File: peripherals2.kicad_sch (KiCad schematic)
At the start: 34 parts, among them J8 MSD-4-A, J9 DISPLAY CONN, Q3 SL2301S, Q4 T2N7002AK,LM, U7 GSDA213

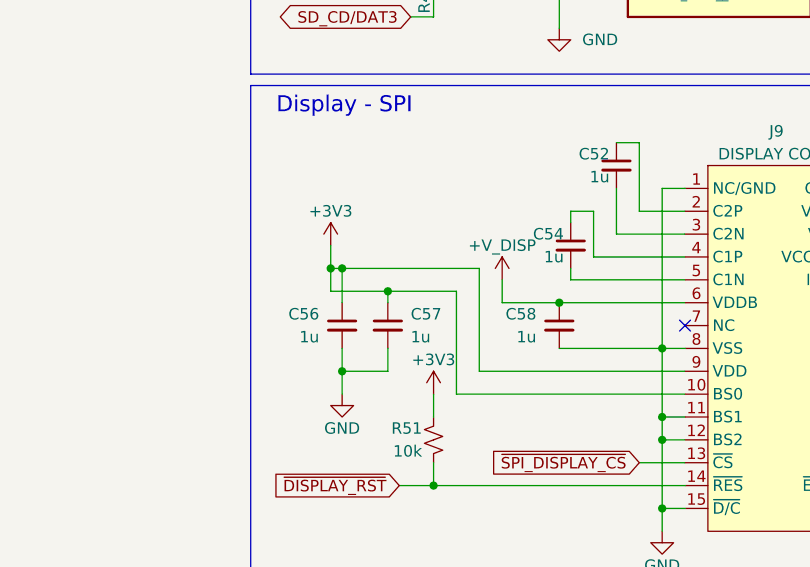
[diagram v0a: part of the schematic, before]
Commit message: Revert "refac: changes peripherals2 placement a bit"
This reverts commit 93e1f0bf6a0797c7dbeceb6b97671e5315e8a9c5.
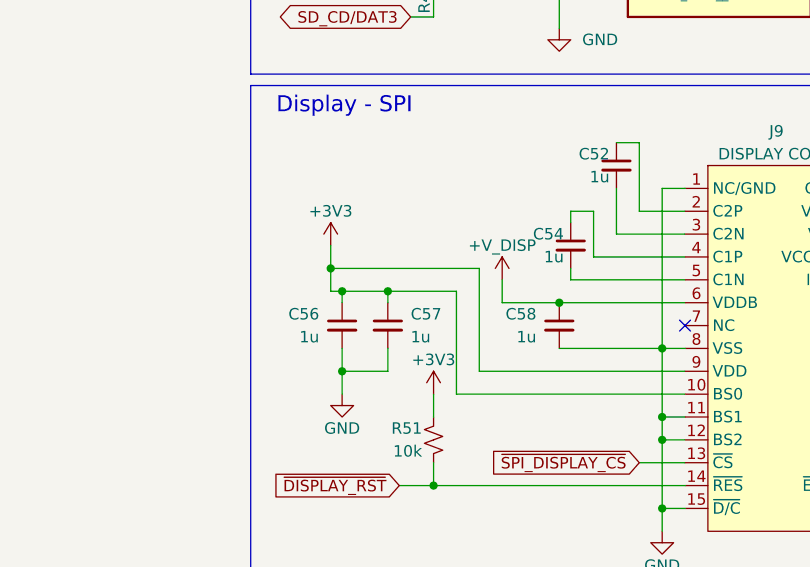
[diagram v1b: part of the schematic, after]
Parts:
- C53: footprint Capacitor_SMD:C_0402_1005Metric -> Capacitor_SMD:C_0603_1608Metric; MPN CL05A225KO5NQNC -> CL10B225KP8NNNC
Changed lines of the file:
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@@
-	)
-	(junction
-		(at 72.39 125.73)
-		(diameter 0)
-		(color 0 0 0 0)
 	)
 	(junction
@@
 	)
 	(junction
+		(at 72.39 128.27)
+		(diameter 0)
+		(color 0 0 0 0)
+	)
+	(junction
 		(at 133.35 119.38)
 		(diameter 0)
@@
 	(wire
 		(pts
-			(xy 72.39 125.73) (xy 87.63 125.73)
-		)
-		(stroke
-			(width 0)
-			(type default)
-		)
-	)
-	(wire
-		(pts
 			(xy 181.61 53.34) (xy 182.88 53.34)
 		)
@@
 	(wire
 		(pts
-			(xy 72.39 125.73) (xy 72.39 129.54)
-		)
-		(stroke
-			(width 0)
-			(type default)
-		)
-	)
-	(wire
-		(pts
 			(xy 130.81 147.32) (xy 135.89 147.32)
 		)
@@
 	(wire
 		(pts
+			(xy 72.39 128.27) (xy 77.47 128.27)
+		)
+		(stroke
+			(width 0)
+			(type default)
+		)
+	)
+	(wire
+		(pts
 			(xy 105.41 111.76) (xy 102.87 111.76)
 		)
@@
 	(wire
 		(pts
-			(xy 71.12 128.27) (xy 77.47 128.27)
+			(xy 71.12 128.27) (xy 72.39 128.27)
 		)
 		(stroke
@@
 	(wire
 		(pts
+			(xy 72.39 128.27) (xy 72.39 129.54)
+		)
+		(stroke
+			(width 0)
+			(type default)
+		)
+	)
+	(wire
+		(pts
 			(xy 158.75 86.36) (xy 149.86 86.36)
 		)
@@
 	(wire
 		(pts
-			(xy 71.12 125.73) (xy 72.39 125.73)
+			(xy 71.12 125.73) (xy 87.63 125.73)
 		)
 		(stroke
@@
 			)
 		)
-		(property "Footprint" "Capacitor_SMD:C_0402_1005Metric"
+		(property "Footprint" "Capacitor_SMD:C_0603_1608Metric"
 			(at 144.78 121.92 0)
 			(effects
@@
 			)
 		)
-		(property "Datasheet" "https://www.digikey.com.br/pt/products/detail/samsung-electro-mechanics/CL05A225KO5NQNC/3887119"
+		(property "Datasheet" "https://www.digikey.com.br/en/products/detail/samsung-electro-mechanics/CL10B225KP8NNNC/3886792"
 			(at 144.78 121.92 0)
 			(effects
@@
 			)
 		)
-		(property "MPN" "CL05A225KO5NQNC"
+		(property "MPN" "CL10B225KP8NNNC"
 			(at 144.78 121.92 0)
 			(effects

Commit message: chore: updates display capacitors
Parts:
- C53: footprint Capacitor_SMD:C_0603_1608Metric -> Capacitor_SMD:C_0402_1005Metric; MPN CL10B225KP8NNNC -> CL05A225KO5NQNC
- C55: MPN CL05A475MP5NRNC -> CL05A105KA5NQNC
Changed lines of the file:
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@@
 			)
 		)
-		(property "Footprint" "Capacitor_SMD:C_0603_1608Metric"
+		(property "Footprint" "Capacitor_SMD:C_0402_1005Metric"
 			(at 144.78 121.92 0)
 			(effects
@@
 			)
 		)
-		(property "Datasheet" "https://www.digikey.com.br/en/products/detail/samsung-electro-mechanics/CL10B225KP8NNNC/3886792"
+		(property "Datasheet" "https://www.digikey.com.br/en/products/detail/samsung-electro-mechanics/CL05A225KO5NQNC/3887119"
 			(at 144.78 121.92 0)
 			(effects
@@
 			)
 		)
-		(property "MPN" "CL10B225KP8NNNC"
+		(property "MPN" "CL05A225KO5NQNC"
 			(at 144.78 121.92 0)
 			(effects
@@
 			)
 		)
-		(property "Datasheet" "https://www.digikey.com.br/en/products/detail/samsung-electro-mechanics/CL05A475MP5NRNC/3887140"
+		(property "Datasheet" "https://www.digikey.com.br/en/products/detail/samsung-electro-mechanics/CL05A105KA5NQNC/3889531"
 			(at 144.78 128.27 0)
 			(effects
@@
 			)
 		)
-		(property "MPN" "CL05A475MP5NRNC"
+		(property "MPN" "CL05A105KA5NQNC"
 			(at 144.78 128.27 0)
 			(effects

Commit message: wip: adds more routing
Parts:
- renumbered C47 to C43, C48 to C44, C49 to C45, C50 to C46, C51 to C47, C52 to C48, C53 to C49, C54 to C50, C55 to C51, C56 to C52, C57 to C53, C58 to C54, J8 to J7, J9 to J8, Q3 to Q4, Q4 to Q5, R44 to R37, R45 to R38, R46 to R39, R47 to R40, R48 to R41, R49 to R42, R50 to R43, R51 to R44, R52 to R45, TP13 to TP12, TP14 to TP13, TP15 to TP14, TP16 to TP15, TP17 to TP16, TP18 to TP17, TP19 to TP18, U7 to U6, U8 to U7

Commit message: refac: aligns all buttons
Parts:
- C51: MPN CL05A105KA5NQNC -> CL05A475MP5NRNC
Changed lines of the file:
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@@
 			)
 		)
-		(property "MPN" "CL05A105KA5NQNC"
+		(property "MPN" "CL05A475MP5NRNC"
 			(at 144.78 128.27 0)
 			(effects

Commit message: refac: changes OR circuit in power supply
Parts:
- renumbered Q4 to Q6, Q5 to Q7, R37 to R38, R38 to R39, R39 to R40, R40 to R41, R41 to R42, R42 to R43, R43 to R44, R44 to R45, R45 to R46, TP12 to TP15, TP13 to TP16, TP14 to TP17, TP15 to TP18, TP16 to TP19, TP17 to TP20, TP18 to TP21

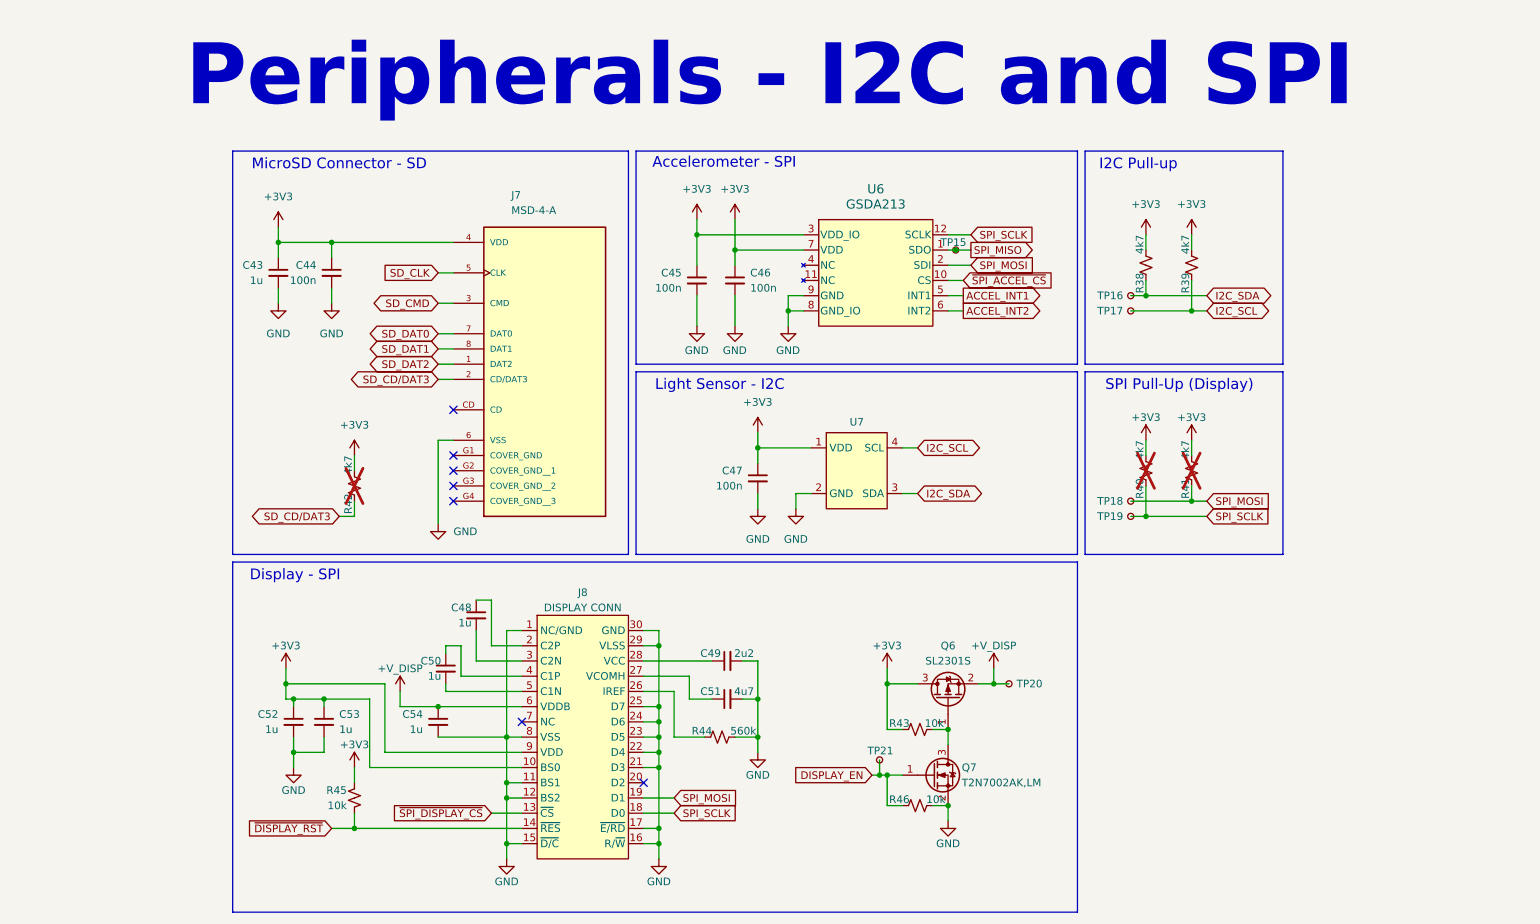
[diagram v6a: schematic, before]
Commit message: feat: adds 4th wire to display, removes remaining sdcard lines
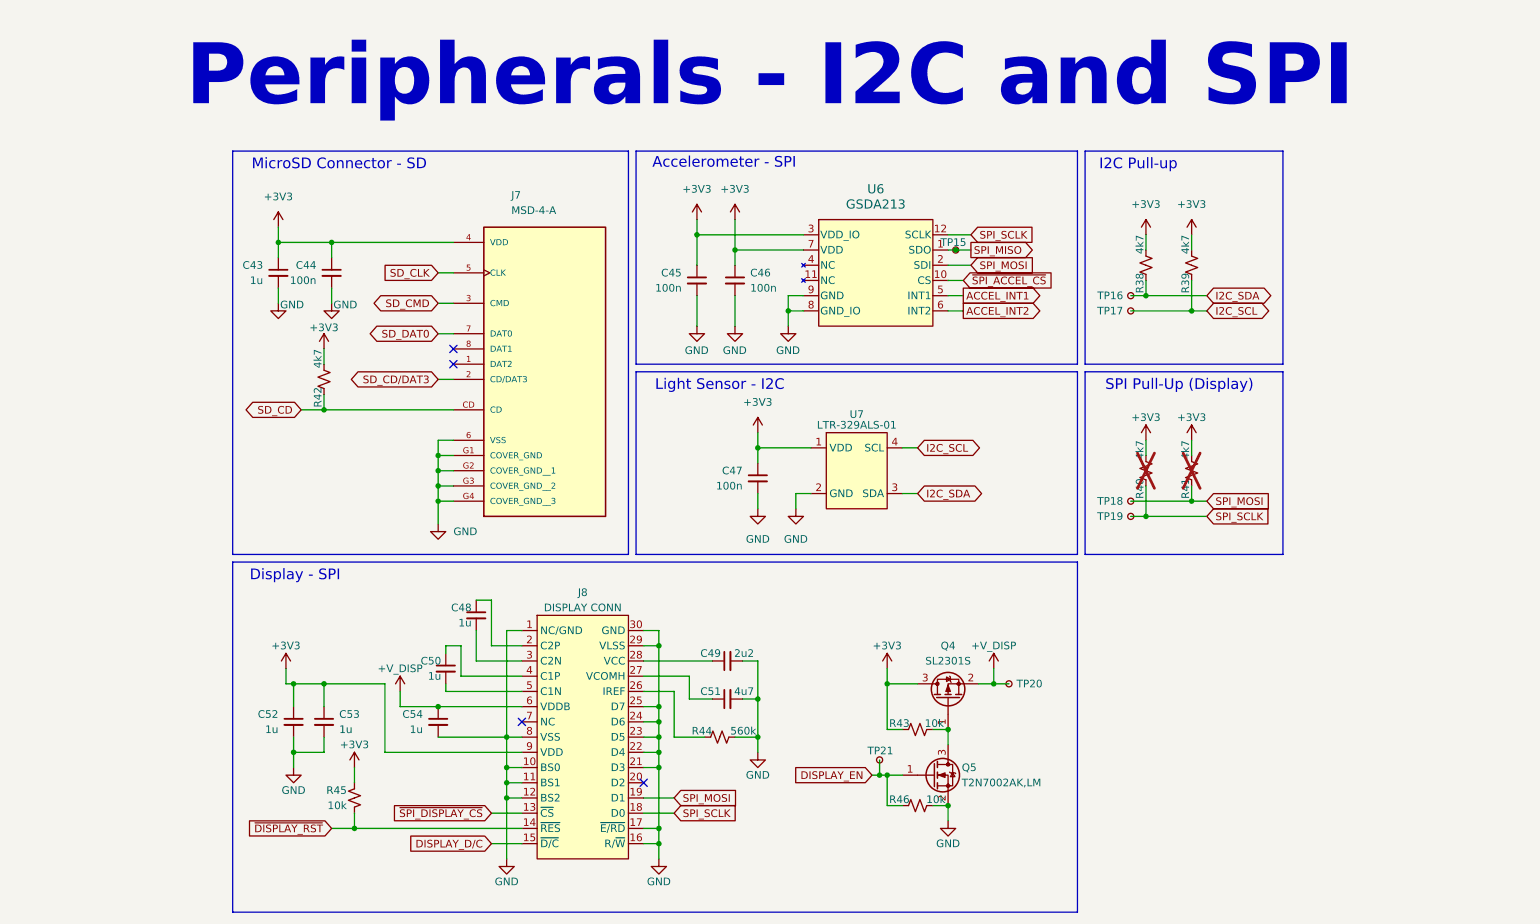
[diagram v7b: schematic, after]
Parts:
- R42: now fitted
- U7: value ~ -> LTR-329ALS-01
- renumbered Q6 to Q4, Q7 to Q5
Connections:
- net +3V3: no longer J8.10 (BS0)
- net GND: now also J7.G1 (COVER_GND), J7.G2 (COVER_GND__1), J7.G3 (COVER_GND__2), J7.G4 (COVER_GND__3), J8.10 (BS0); no longer J8.15 (~{D/C})
- net SD_CD/DAT3: no longer R42.1
- net SD_CD: now reaches J7.CD
- net SD_CD: now also R42.1
- net SD_DAT1: no longer names the net of J7.8 (DAT1)
- net SD_DAT2: no longer names the net of J7.1 (DAT2)
- new net DISPLAY_D/C: J8.15 (~{D/C})
- no-connect marks 7 -> 4

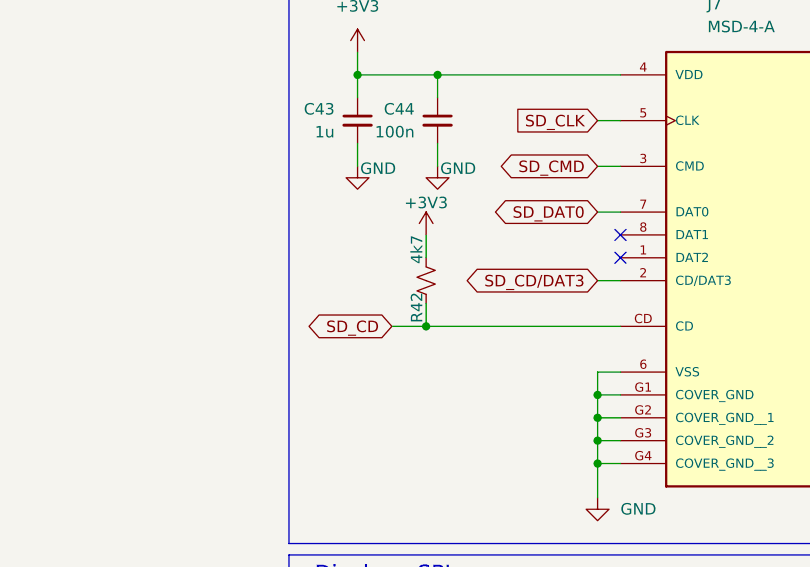
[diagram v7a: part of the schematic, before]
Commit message: fix: removes solder past layer from display conn
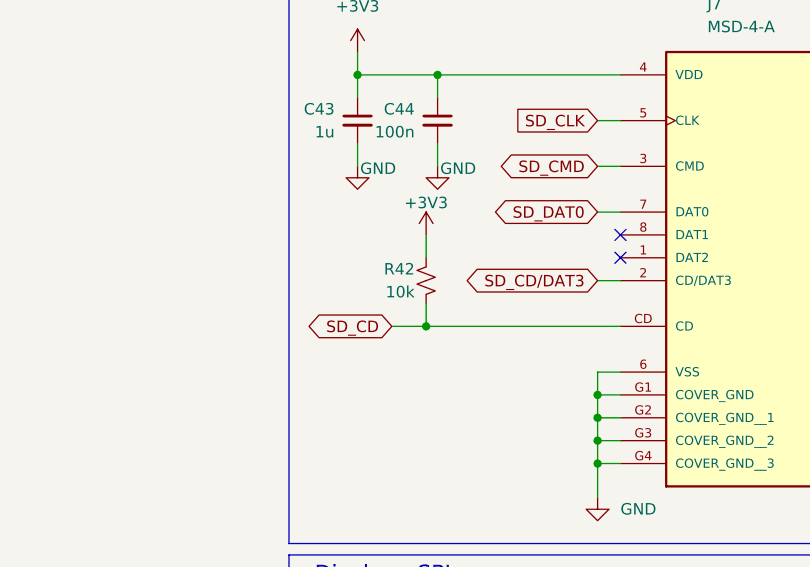
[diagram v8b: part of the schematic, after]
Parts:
- R42: value 4k7 -> 10k; MPN RC0402JR-074K7L -> RC0402JR-0710KL
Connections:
- net +3V3: now also R42.1; no longer R42.2
- net SD_CD: now also R42.2; no longer R42.1
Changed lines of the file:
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@@
+	)
+	(symbol
+		(lib_id "Device:R_Small_US")
+		(at 77.47 74.93 0)
+		(mirror y)
+		(unit 1)
+		(exclude_from_sim no)
+		(in_bom yes)
+		(on_board yes)
+		(dnp no)
+		(property "Reference" "R42"
+			(at 76.2 73.66 0)
+			(effects
+				(font
+					(size 1.27 1.27)
+				)
+				(justify left)
+			)
+		)
+		(property "Value" "10k"
+			(at 76.2 76.2 0)
+			(effects
+				(font
+					(size 1.27 1.27)
+				)
+				(justify left)
+			)
+		)
+		(property "Footprint" "Resistor_SMD:R_0402_1005Metric"
+			(at 77.47 74.93 0)
+			(effects
+				(font
+					(size 1.27 1.27)
+				)
+				(hide yes)
+			)
+		)
+		(property "Datasheet" "https://www.digikey.com.br/en/products/detail/yageo/RC0402JR-0710KL/726418?s=N4IgTCBcDaIEoGEAMAWJYBScC0SDsAjEgNIAyIAugL5A"
+			(at 77.47 74.93 0)
+			(effects
+				(font
+					(size 1.27 1.27)
+				)
+				(hide yes)
+			)
+		)
+		(property "Description" "Resistor, small US symbol"
+			(at 77.47 74.93 0)
+			(effects
+				(font
+					(size 1.27 1.27)
+				)
+				(hide yes)
+			)
+		)
+		(property "MPN" "RC0402JR-0710KL"
+			(at 77.47 74.93 0)
+			(effects
+				(font
+					(size 1.27 1.27)
+				)
+				(hide yes)
+			)
+		)
+		(property "Availability" ""
+			(at 77.47 74.93 0)
+			(effects
+				(font
+					(size 1.27 1.27)
+				)
+				(hide yes)
+			)
+		)
+		(property "Check_prices" ""
+			(at 77.47 74.93 0)
+			(effects
+				(font
+					(size 1.27 1.27)
+				)
+				(hide yes)
+			)
+		)
+		(property "Description_1" ""
+			(at 77.47 74.93 0)
+			(effects
+				(font
+					(size 1.27 1.27)
+				)
+				(hide yes)
+			)
+		)
+		(property "MF" ""
+			(at 77.47 74.93 0)
+			(effects
+				(font
+					(size 1.27 1.27)
+				)
+				(hide yes)
+			)
+		)
+		(property "Package" ""
+			(at 77.47 74.93 0)
+			(effects
+				(font
+					(size 1.27 1.27)
+				)
+				(hide yes)
+			)
+		)
+		(property "Price" ""
+			(at 77.47 74.93 0)
+			(effects
+				(font
+					(size 1.27 1.27)
+				)
+				(hide yes)
+			)
+		)
+		(property "SnapEDA_Link" ""
+			(at 77.47 74.93 0)
+			(effects
+				(font
+					(size 1.27 1.27)
+				)
+				(hide yes)
+			)
+		)
+		(pin "2"
+		)
+		(pin "1"
+		)
+		(instances
+			(project "zbook"
+				(path "/b90666d0-8852-4bb1-832d-f9d855027372/e26c05ee-f364-47de-be04-e77902e037c8"
+					(reference "R42")
+					(unit 1)
+				)
+			)
+		)
 	)
 	(symbol
@@
 					(unit 1)
 				)
-			)
-		)
-	)
-	(symbol
-		(lib_id "Device:R_Small_US")
-		(at 77.47 74.93 180)
-		(unit 1)
-		(exclude_from_sim no)
-		(in_bom yes)
-		(on_board yes)
-		(dnp no)
-		(property "Reference" "R42"
-			(at 76.454 76.2 90)
-			(effects
-				(font
-					(size 1.27 1.27)
-				)
-				(justify left)
-			)
-		)
-		(property "Value" "4k7"
-			(at 76.454 69.85 90)
-			(effects
-				(font
-					(size 1.27 1.27)
-				)
-				(justify left)
-			)
-		)
-		(property "Footprint" "Resistor_SMD:R_0402_1005Metric"
-			(at 77.47 74.93 0)
-			(effects
-				(font
-					(size 1.27 1.27)
-				)
-				(hide yes)
-			)
-		)
-		(property "Datasheet" "https://www.digikey.com.br/en/products/detail/yageo/RC0402JR-074K7L/726477"
-			(at 77.47 74.93 0)
-			(effects
-				(font
-					(size 1.27 1.27)
-				)
-				(hide yes)
-			)
-		)
-		(property "Description" "Resistor, small US symbol"
-			(at 77.47 74.93 0)
-			(effects
-				(font
-					(size 1.27 1.27)
-				)
-				(hide yes)
-			)
-		)
-		(property "MPN" "RC0402JR-074K7L"
-			(at 77.47 74.93 0)
-			(effects
-				(font
-					(size 1.27 1.27)
-				)
-				(hide yes)
-			)
-		)
-		(property "Availability" ""
-			(at 77.47 74.93 90)
-			(effects
-				(font
-					(size 1.27 1.27)
-				)
-				(hide yes)
-			)
-		)
-		(property "Check_prices" ""
-			(at 77.47 74.93 90)
-			(effects
-				(font
-					(size 1.27 1.27)
-				)
-				(hide yes)
-			)
-		)
-		(property "Description_1" ""
-			(at 77.47 74.93 90)
-			(effects
-				(font
-					(size 1.27 1.27)
-				)
-				(hide yes)
-			)
-		)
-		(property "MF" ""
-			(at 77.47 74.93 90)
-			(effects
-				(font
-					(size 1.27 1.27)
-				)
-				(hide yes)
-			)
-		)
-		(property "Package" ""
-			(at 77.47 74.93 90)
-			(effects
-				(font
-					(size 1.27 1.27)
-				)
-				(hide yes)
-			)
-		)
-		(property "Price" ""
-			(at 77.47 74.93 90)
-			(effects
-				(font
-					(size 1.27 1.27)
-				)
-				(hide yes)
-			)
-		)
-		(property "SnapEDA_Link" ""
-			(at 77.47 74.93 90)
-			(effects
-				(font
-					(size 1.27 1.27)
-				)
-				(hide yes)
-			)
-		)
-		(pin "2"
-		)
-		(pin "1"
-		)
-		(instances
-			(project "zbook"
-				(path "/b90666d0-8852-4bb1-832d-f9d855027372/e26c05ee-f364-47de-be04-e77902e037c8"
-					(reference "R42")
-					(unit 1)
-				)
